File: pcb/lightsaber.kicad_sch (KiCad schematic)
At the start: 66 parts, among them IC1 BMI055, J1 2012670005, J2 Screw_Terminal_01x05, J3 ESP32 Prog, J4 ESP32 JTAG, J5 Conn_01x02, J6 Conn_01x06, Q1 PMOS, Q2 NPN, SW1 SW_Push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

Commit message: Tidying up routing
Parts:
- D4, U2: now left out of the parts list
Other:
- moved on the sheet: C25, D6, U7

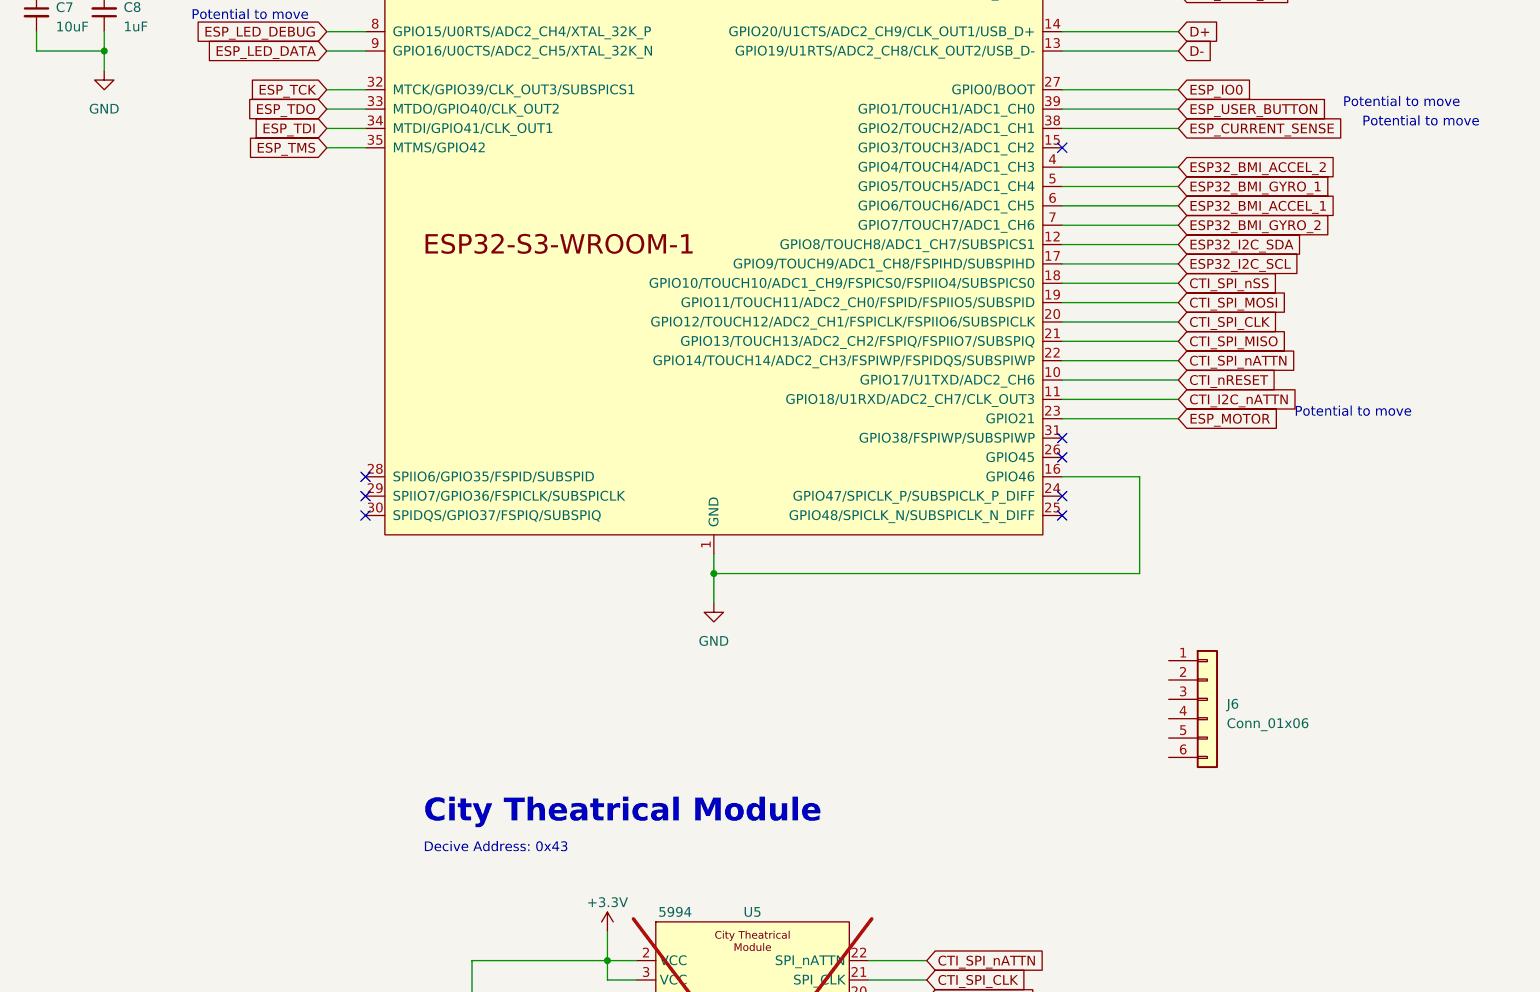
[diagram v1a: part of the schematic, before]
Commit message: Adding external IO
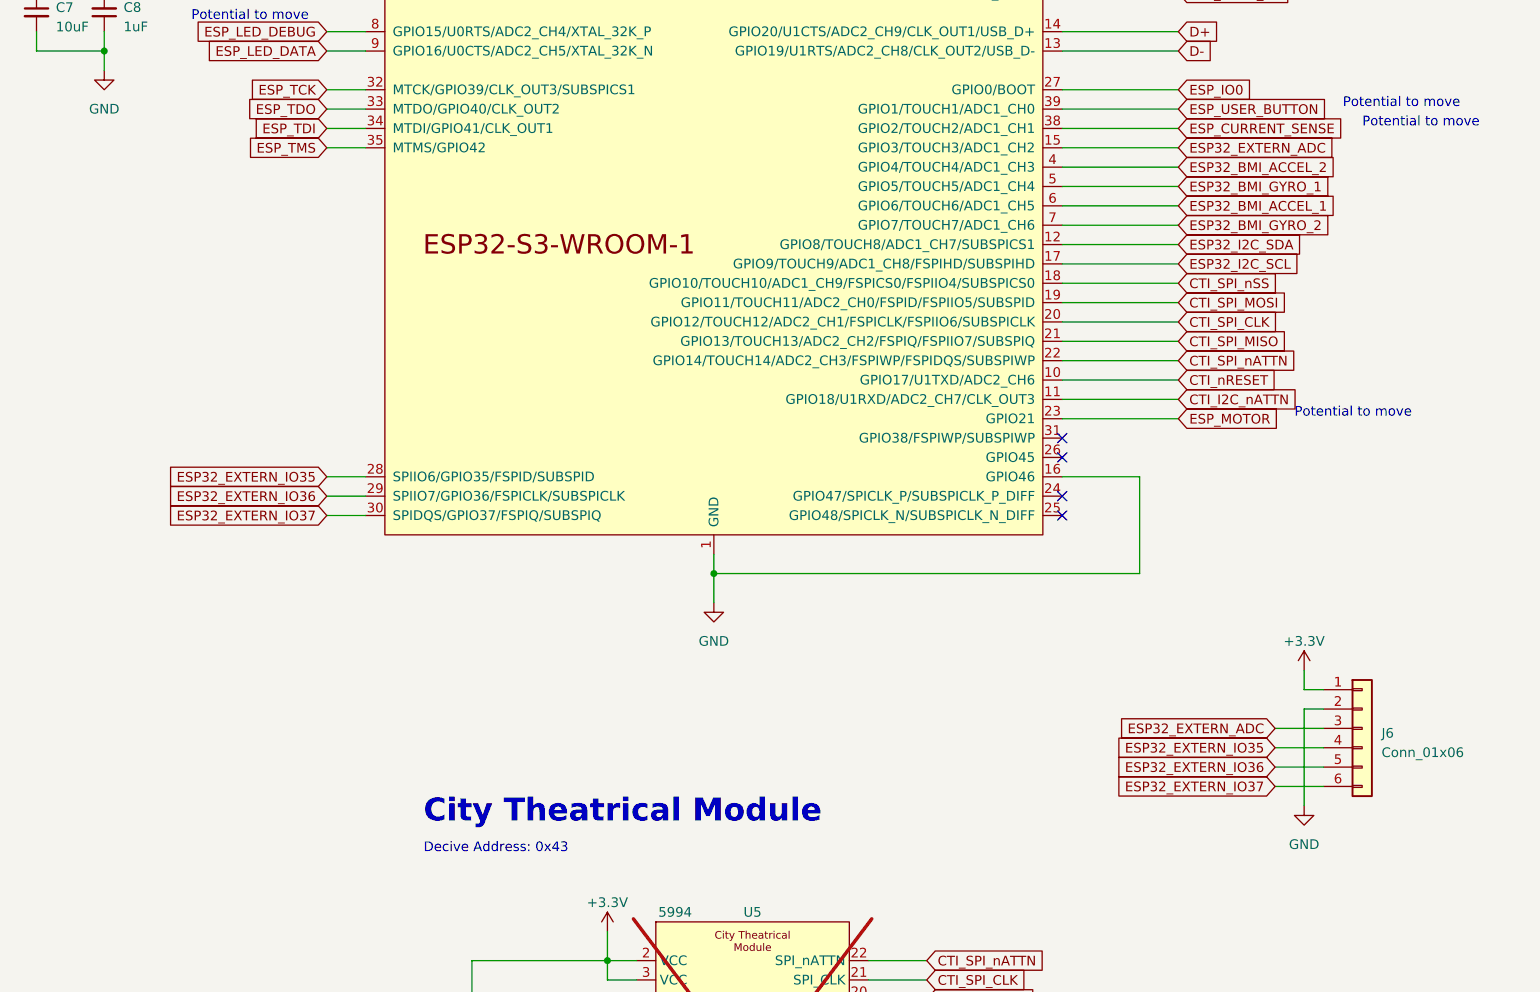
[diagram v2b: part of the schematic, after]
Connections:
- net +3.3V: now also J6.1 (Pin_1)
- net GND: now also J6.2 (Pin_2)
- net ESP32_EXTERN_ADC: now reaches U2.15 (GPIO3/TOUCH3/ADC1_CH2)
- net ESP32_EXTERN_ADC: now also J6.3 (Pin_3)
- net ESP32_EXTERN_IO35: now reaches U2.28 (SPIIO6/GPIO35/FSPID/SUBSPID)
- net ESP32_EXTERN_IO35: now also J6.4 (Pin_4)
- net ESP32_EXTERN_IO36: now reaches U2.29 (SPIIO7/GPIO36/FSPICLK/SUBSPICLK)
- net ESP32_EXTERN_IO36: now also J6.5 (Pin_5)
- net ESP32_EXTERN_IO37: now reaches U2.30 (SPIDQS/GPIO37/FSPIQ/SUBSPIQ)
- net ESP32_EXTERN_IO37: now also J6.6 (Pin_6)
- no-connect marks 28 -> 24
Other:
- moved on the sheet: J6
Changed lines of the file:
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@@
   (no_connect (at 36.83 59.69))
   (no_connect (at 36.83 54.61))
-  (no_connect (at 421.64 115.57))
-  (no_connect (at 421.64 110.49))
   (no_connect (at 36.83 31.75))
   (no_connect (at 323.85 265.43))
@@
   (no_connect (at 300.99 124.46))
   (no_connect (at 513.08 107.95))
-  (no_connect (at 421.64 113.03))
-  (no_connect (at 513.08 67.31))
   (no_connect (at 513.08 105.41))
   (no_connect (at 113.03 189.23))
@@
     (stroke (width 0) (type default))
   )
+  (wire (pts (xy 544.83 138.43) (xy 547.37 138.43))
+    (stroke (width 0) (type default))
+  )
   (wire (pts (xy 478.79 212.09) (xy 476.25 212.09))
     (stroke (width 0) (type default))
@@
     (stroke (width 0) (type default))
   )
+  (wire (pts (xy 544.83 140.97) (xy 544.83 153.67))
+    (stroke (width 0) (type default))
+  )
   (wire (pts (xy 513.08 82.55) (xy 528.32 82.55))
     (stroke (width 0) (type default))
@@
     (stroke (width 0) (type default))
   )
+  (wire (pts (xy 544.83 140.97) (xy 547.37 140.97))
+    (stroke (width 0) (type default))
+  )
   (wire (pts (xy 487.68 181.61) (xy 495.3 181.61))
     (stroke (width 0) (type default))
@@
     (stroke (width 0) (type default))
   )
+  (wire (pts (xy 513.08 67.31) (xy 528.32 67.31))
+    (stroke (width 0) (type default))
+  )
   (wire (pts (xy 198.12 132.08) (xy 198.12 137.16))
     (stroke (width 0) (type default))
@@
     (stroke (width 0) (type default))
   )
+  (wire (pts (xy 416.56 113.03) (xy 421.64 113.03))
+    (stroke (width 0) (type default))
+  )
   (wire (pts (xy 99.06 31.75) (xy 101.6 31.75))
     (stroke (width 0) (type default))
@@
     (stroke (width 0) (type default))
   )
+  (wire (pts (xy 541.02 146.05) (xy 547.37 146.05))
+    (stroke (width 0) (type default))
+  )
   (wire (pts (xy 513.08 77.47) (xy 528.32 77.47))
     (stroke (width 0) (type default))
   )
+  (wire (pts (xy 541.02 143.51) (xy 547.37 143.51))
+    (stroke (width 0) (type default))
+  )
   (wire (pts (xy 198.12 137.16) (xy 198.12 140.97))
     (stroke (width 0) (type default))
@@
     (stroke (width 0) (type default))
   )
+  (wire (pts (xy 416.56 110.49) (xy 421.64 110.49))
+    (stroke (width 0) (type default))
+  )
   (wire (pts (xy 74.93 59.69) (xy 74.93 62.23))
     (stroke (width 0) (type default))
@@
     (stroke (width 0) (type default))
   )
+  (wire (pts (xy 541.02 151.13) (xy 547.37 151.13))
+    (stroke (width 0) (type default))
+  )
   (wire (pts (xy 513.08 92.71) (xy 528.32 92.71))
     (stroke (width 0) (type default))
@@
     (stroke (width 0) (type default))
   )
+  (wire (pts (xy 416.56 115.57) (xy 421.64 115.57))
+    (stroke (width 0) (type default))
+  )
   (wire (pts (xy 411.48 256.54) (xy 414.02 256.54))
     (stroke (width 0) (type default))
@@
     (stroke (width 0) (type default))
   )
+  (wire (pts (xy 541.02 148.59) (xy 547.37 148.59))
+    (stroke (width 0) (type default))
+  )
   (wire (pts (xy 350.52 111.76) (xy 350.52 114.3))
     (stroke (width 0) (type default))
@@
     (stroke (width 0) (type default))
   )
+  (wire (pts (xy 544.83 135.89) (xy 544.83 138.43))
+    (stroke (width 0) (type default))
+  )
   (wire (pts (xy 134.62 31.75) (xy 134.62 25.4))
     (stroke (width 0) (type default))
@@
     )
   )
+  (global_label "ESP32_EXTERN_IO37" (shape input) (at 416.56 115.57 180) (fields_autoplaced)
+    (effects (font (size 1.27 1.27)) (justify right))
+    (property "Intersheetrefs" "${INTERSHEET_REFS}" (at 394.2416 115.57 0)
+      (effects (font (size 1.27 1.27)) (justify right) hide)
+    )
+  )
   (global_label "CTI_SPI_MOSI" (shape input) (at 528.32 87.63 0) (fields_autoplaced)
     (effects (font (size 1.27 1.27)) (justify left))
@@
     )
   )
+  (global_label "ESP32_EXTERN_IO36" (shape input) (at 541.02 148.59 180) (fields_autoplaced)
+    (effects (font (size 1.27 1.27)) (justify right))
+    (property "Intersheetrefs" "${INTERSHEET_REFS}" (at 518.7016 148.59 0)
+      (effects (font (size 1.27 1.27)) (justify right) hide)
+    )
+  )
   (global_label "ESP32_BMI_GYRO_1" (shape input) (at 528.32 72.39 0) (fields_autoplaced)
     (effects (font (size 1.27 1.27)) (justify left))
@@
     )
   )
+  (global_label "ESP32_EXTERN_ADC" (shape input) (at 528.32 67.31 0) (fields_autoplaced)
+    (effects (font (size 1.27 1.27)) (justify left))
+    (property "Intersheetrefs" "${INTERSHEET_REFS}" (at 549.9127 67.31 0)
+      (effects (font (size 1.27 1.27)) (justify left) hide)
+    )
+  )
   (global_label "ESP_LED_DEBUG" (shape input) (at 304.8 265.43 180) (fields_autoplaced)
     (effects (font (size 1.27 1.27)) (justify right))
@@
     )
   )
+  (global_label "ESP32_EXTERN_IO37" (shape input) (at 541.02 151.13 180) (fields_autoplaced)
+    (effects (font (size 1.27 1.27)) (justify right))
+    (property "Intersheetrefs" "${INTERSHEET_REFS}" (at 518.7016 151.13 0)
+      (effects (font (size 1.27 1.27)) (justify right) hide)
+    )
+  )
+  (global_label "ESP32_EXTERN_IO35" (shape input) (at 416.56 110.49 180) (fields_autoplaced)
+    (effects (font (size 1.27 1.27)) (justify right))
+    (property "Intersheetrefs" "${INTERSHEET_REFS}" (at 394.2416 110.49 0)
+      (effects (font (size 1.27 1.27)) (justify right) hide)
+    )
+  )
   (global_label "CTI_SPI_nSS" (shape input) (at 528.32 85.09 0) (fields_autoplaced)
     (effects (font (size 1.27 1.27)) (justify left))
@@
     )
   )
+  (global_label "ESP32_EXTERN_ADC" (shape input) (at 541.02 143.51 180) (fields_autoplaced)
+    (effects (font (size 1.27 1.27)) (justify right))
+    (property "Intersheetrefs" "${INTERSHEET_REFS}" (at 519.4273 143.51 0)
+      (effects (font (size 1.27 1.27)) (justify right) hide)
+    )
+  )
   (global_label "ESP_TDO" (shape input) (at 416.56 62.23 180) (fields_autoplaced)
     (effects (font (size 1.27 1.27)) (justify right))
@@
     )
   )
+  (global_label "ESP32_EXTERN_IO36" (shape input) (at 416.56 113.03 180) (fields_autoplaced)
+    (effects (font (size 1.27 1.27)) (justify right))
+    (property "Intersheetrefs" "${INTERSHEET_REFS}" (at 394.2416 113.03 0)
+      (effects (font (size 1.27 1.27)) (justify right) hide)
+    )
+  )
   (global_label "ESP32_BMI_GYRO_1" (shape input) (at 331.47 119.38 0) (fields_autoplaced)
     (effects (font (size 1.27 1.27)) (justify left))
@@
     )
   )
+  (global_label "ESP32_EXTERN_IO35" (shape input) (at 541.02 146.05 180) (fields_autoplaced)
+    (effects (font (size 1.27 1.27)) (justify right))
+    (property "Intersheetrefs" "${INTERSHEET_REFS}" (at 518.7016 146.05 0)
+      (effects (font (size 1.27 1.27)) (justify right) hide)
+    )
+  )
   (global_label "CTI_nRESET" (shape input) (at 528.32 97.79 0) (fields_autoplaced)
     (effects (font (size 1.27 1.27)) (justify left))
@@
     )
   )
+  (symbol (lib_id "power:+3.3V") (at 544.83 135.89 0) (unit 1)
+    (in_bom yes) (on_board yes) (dnp no) (fields_autoplaced)
+    (property "Reference" "#PWR039" (at 544.83 139.7 0)
+      (effects (font (size 1.27 1.27)) hide)
+    )
+    (property "Value" "+3.3V" (at 544.83 132.08 0)
+      (effects (font (size 1.27 1.27)))
+    )
+    (property "Footprint" "" (at 544.83 135.89 0)
+      (effects (font (size 1.27 1.27)) hide)
+    )
+    (property "Datasheet" "" (at 544.83 135.89 0)
+      (effects (font (size 1.27 1.27)) hide)
+    )
+    (pin "1")
+    (instances
+      (project "lightsaber"
+        (path "/480b6f8b-587f-4642-8a87-aec0c171ba44"
+          (reference "#PWR039") (unit 1)
+        )
+      )
+      (project "CTI_ESP32"
+        (path "/6d3948e0-7215-4b5f-a564-64550d12cd9d"
+          (reference "#PWR04") (unit 1)
+        )
+      )
+    )
+  )
   (symbol (lib_id "power:VDD") (at 226.06 53.34 0) (unit 1)
     (in_bom yes) (on_board yes) (dnp no) (fields_autoplaced)
@@
     )
   )
+  (symbol (lib_id "power:GND") (at 544.83 153.67 0) (unit 1)
+    (in_bom yes) (on_board yes) (dnp no) (fields_autoplaced)
+    (property "Reference" "#PWR050" (at 544.83 160.02 0)
+      (effects (font (size 1.27 1.27)) hide)
+    )
+    (property "Value" "GND" (at 544.83 158.75 0)
+      (effects (font (size 1.27 1.27)))
+    )
+    (property "Footprint" "" (at 544.83 153.67 0)
+      (effects (font (size 1.27 1.27)) hide)
+    )
+    (property "Datasheet" "" (at 544.83 153.67 0)
+      (effects (font (size 1.27 1.27)) hide)
+    )
+    (pin "1")
+    (instances
+      (project "lightsaber"
+        (path "/480b6f8b-587f-4642-8a87-aec0c171ba44"
+          (reference "#PWR050") (unit 1)
+        )
+      )
+      (project "CTI_ESP32"
+        (path "/6d3948e0-7215-4b5f-a564-64550d12cd9d"
+          (reference "#PWR027") (unit 1)
+        )
+      )
+    )
+  )
   (symbol (lib_id "Device:C_Small") (at 350.52 109.22 0) (unit 1)
     (in_bom yes) (on_board yes) (dnp no) (fields_autoplaced)
@@
     )
   )
-  (symbol (lib_id "Connector_Generic:Conn_01x06") (at 532.13 139.7 0) (unit 1)
+  (symbol (lib_id "Connector_Generic:Conn_01x06") (at 552.45 143.51 0) (unit 1)
     (in_bom yes) (on_board yes) (dnp no) (fields_autoplaced)
-    (property "Reference" "J6" (at 534.67 140.335 0)
+    (property "Reference" "J6" (at 554.99 144.145 0)
       (effects (font (size 1.27 1.27)) (justify left))
     )
-    (property "Value" "Conn_01x06" (at 534.67 142.875 0)
+    (property "Value" "Conn_01x06" (at 554.99 146.685 0)
       (effects (font (size 1.27 1.27)) (justify left))
     )
-    (property "Footprint" "Connector_PinHeader_2.54mm:PinHeader_1x06_P2.54mm_Vertical" (at 532.13 139.7 0)
+    (property "Footprint" "Connector_PinHeader_2.54mm:PinHeader_1x06_P2.54mm_Vertical" (at 552.45 143.51 0)
       (effects (font (size 1.27 1.27)) hide)
     )
-    (property "Datasheet" "~" (at 532.13 139.7 0)
+    (property "Datasheet" "~" (at 552.45 143.51 0)
       (effects (font (size 1.27 1.27)) hide)
     )
